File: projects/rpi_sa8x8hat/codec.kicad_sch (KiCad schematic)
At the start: 24 parts, among them U4 TLV320AIC3204

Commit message: WIP.
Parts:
- removed TP2, TP3, TP4, TP5, TP6: TestPoint, symbol Connector:TestPoint
- C10, C11, C15, C6, C8: footprint (none) -> Capacitor_SMD:C_0201_0603Metric
- C14, C20, C4, C5, C7, C9: footprint (none) -> Capacitor_SMD:C_0402_1005Metric
- R10, R11, R12, R14, R8, R9: footprint (none) -> Resistor_SMD:R_0402_1005Metric
- TP1: footprint (none) -> TestPoint:TestPoint_Pad_2.0x2.0mm

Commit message: .
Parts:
- removed TP1: TestPoint, TestPoint:TestPoint_Pad_2.0x2.0mm, symbol Connector:TestPoint
- renumbered C20 to C10, C4 to C11, C5 to C12, C6 to C13, C7 to C14, C9 to C15, C8 to C16, C10 to C17, C11 to C18, C14 to C19, C15 to C20, R8 to R12, R9 to R13, R10 to R14, R11 to R15, R14 to R16, R12 to R17, U4 to U3
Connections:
- no-connect marks 5 -> 6

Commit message: WIP.  Rought 2L layout; prolly will switch to 4L.
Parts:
- added TP1, TP10, TP11, TP12, TP13, TP16, TP2, TP7, TP8, TP9: TestPoint, TestPoint:TestPoint_Pad_D1.0mm, symbol Connector:TestPoint
- C13, C16, C17, C18, C20: footprint Capacitor_SMD:C_0201_0603Metric -> Capacitor_SMD:C_0402_1005Metric
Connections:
- net I2S_BCLK: now also TP12.1
- net I2S_CLK_25MHZ: now also TP13.1
- net I2S_IN: now also TP9.1
- net I2S_OUT: now also TP10.1
- net I2S_WCLK: now also TP11.1
- net IN1_L: now also TP1.1
- net IN1_R: now also TP2.1
- net LOL: now also TP7.1
- net LOR: now also TP8.1
- net ~{RESET}: now also TP16.1

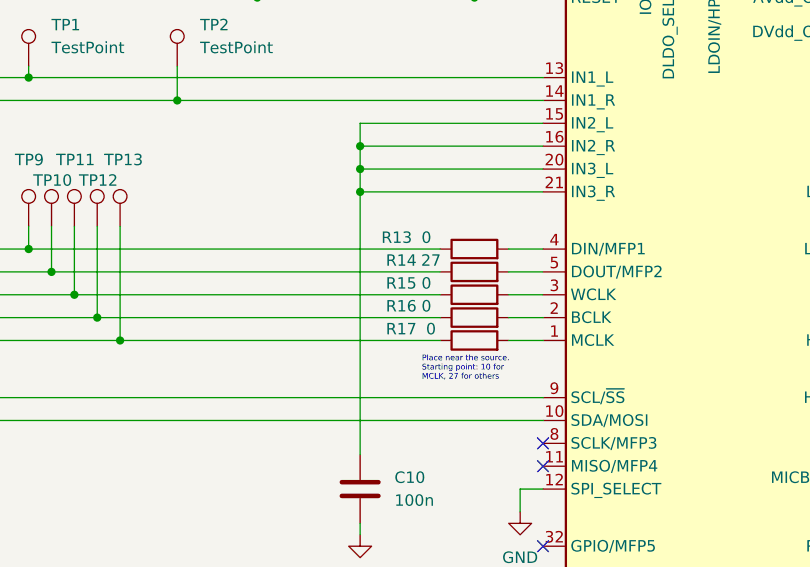
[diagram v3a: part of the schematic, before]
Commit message: Fix I2S series resistor values.
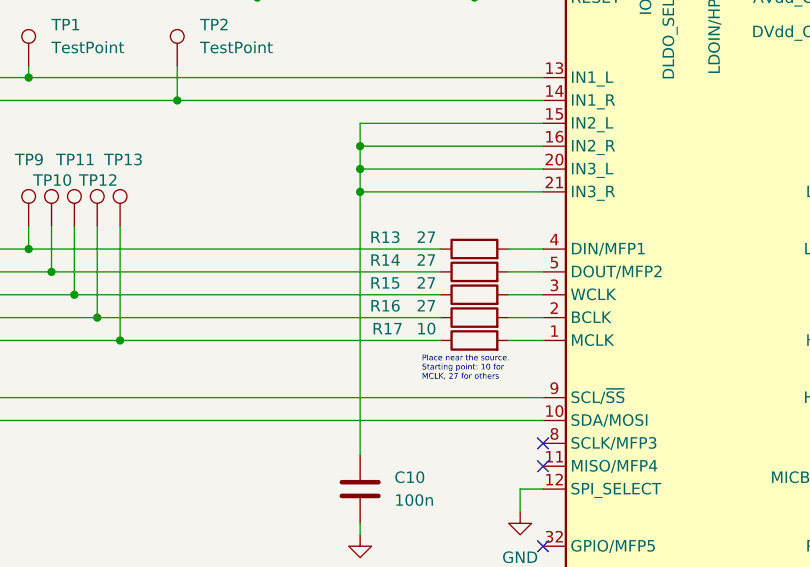
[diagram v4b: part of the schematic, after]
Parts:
- R13, R15, R16: value 0 -> 27
- R17: value 0 -> 10
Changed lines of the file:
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@@
 		(dnp no)
 		(property "Reference" "R15"
-			(at 94.742 88.9 90)
-			(effects
-				(font
-					(size 1.27 1.27)
-				)
-			)
-		)
-		(property "Value" "0"
+			(at 92.964 88.9 90)
+			(effects
+				(font
+					(size 1.27 1.27)
+				)
+			)
+		)
+		(property "Value" "27"
 			(at 97.536 88.9 90)
 			(effects
@@
 		(dnp no)
 		(property "Reference" "R17"
-			(at 94.742 93.98 90)
-			(effects
-				(font
-					(size 1.27 1.27)
-				)
-			)
-		)
-		(property "Value" "0"
-			(at 98.044 93.98 90)
+			(at 93.218 93.98 90)
+			(effects
+				(font
+					(size 1.27 1.27)
+				)
+			)
+		)
+		(property "Value" "10"
+			(at 97.536 93.98 90)
 			(effects
 				(font
@@
 		(dnp no)
 		(property "Reference" "R14"
-			(at 94.742 86.36 90)
+			(at 92.964 86.36 90)
 			(effects
 				(font
@@
 		)
 		(property "Value" "27"
-			(at 98.044 86.36 90)
+			(at 97.536 86.36 90)
 			(effects
 				(font
@@
 		(dnp no)
 		(property "Reference" "R16"
-			(at 94.742 91.44 90)
-			(effects
-				(font
-					(size 1.27 1.27)
-				)
-			)
-		)
-		(property "Value" "0"
+			(at 92.964 91.44 90)
+			(effects
+				(font
+					(size 1.27 1.27)
+				)
+			)
+		)
+		(property "Value" "27"
 			(at 97.536 91.44 90)
 			(effects
@@
 		(dnp no)
 		(property "Reference" "R13"
-			(at 94.234 83.82 90)
-			(effects
-				(font
-					(size 1.27 1.27)
-				)
-			)
-		)
-		(property "Value" "0"
+			(at 92.964 83.82 90)
+			(effects
+				(font
+					(size 1.27 1.27)
+				)
+			)
+		)
+		(property "Value" "27"
 			(at 97.536 83.82 90)
 			(effects

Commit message: wip
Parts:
- R12, R13, R14, R15, R16, R17: footprint Resistor_SMD:R_0402_1005Metric -> Resistor_SMD:R_0201_0603Metric
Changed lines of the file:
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@@
 			)
 		)
-		(property "Footprint" "Resistor_SMD:R_0402_1005Metric"
+		(property "Footprint" "Resistor_SMD:R_0201_0603Metric"
 			(at 102.87 91.948 90)
 			(effects
@@
 			)
 		)
-		(property "Footprint" "Resistor_SMD:R_0402_1005Metric"
+		(property "Footprint" "Resistor_SMD:R_0201_0603Metric"
 			(at 102.87 97.028 90)
 			(effects
@@
 			)
 		)
-		(property "Footprint" "Resistor_SMD:R_0402_1005Metric"
+		(property "Footprint" "Resistor_SMD:R_0201_0603Metric"
 			(at 102.87 89.408 90)
 			(effects
@@
 			)
 		)
-		(property "Footprint" "Resistor_SMD:R_0402_1005Metric"
+		(property "Footprint" "Resistor_SMD:R_0201_0603Metric"
 			(at 101.092 52.07 90)
 			(effects
@@
 			)
 		)
-		(property "Footprint" "Resistor_SMD:R_0402_1005Metric"
+		(property "Footprint" "Resistor_SMD:R_0201_0603Metric"
 			(at 102.87 94.488 90)
 			(effects
@@
 			)
 		)
-		(property "Footprint" "Resistor_SMD:R_0402_1005Metric"
+		(property "Footprint" "Resistor_SMD:R_0201_0603Metric"
 			(at 102.87 86.868 90)
 			(effects
